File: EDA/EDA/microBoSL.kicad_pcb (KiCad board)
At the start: 4 copper layers, 40 x 13 mm, 54 parts, among them J1 Conn_01x04, J2 Conn_02x03_Odd_Even, J3 Conn_01x04, J4 Conn_01x04, J5 Conn_01x02, J6 Conn_01x10, J7 Conn_01x02, J8 USB_B_Micro, Q1 DMG2302UK, SW1 PTS636 SM43J SMTR LFS, U1 MAX40200ANS, U2 MAX40200ANS, U3 MCP1700-3302E_SOT23, U4 ATmega328-MMH, U5 MCP7940N-xSN, U6 74HC126PW-Q100, U7 FT232RQ, U8 Si4463, Y1 8MHz, Y2 32.768 kHz, Y3 30 MHz

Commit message: moved location on pcb of si4463
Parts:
- C10, C12: value C -> 5.1 pF
- C11: value C -> 6.8 pF
- C13: value C -> 12 pF
- C14: value C -> 18 pF
- C15: value C -> 9.1 pF
- L1: value L -> 220 nH
- L2: value L -> 68 nH
- L3: value L -> 24 nH
- L4: value L -> 27 nH
- L5, L6: value L -> 12 nH
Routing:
- net unconnected-(J6-Pad5): track 0.00 -> 13.1 mm, vias 0 -> 1
- net SS: track 13.1 -> 0.00 mm, vias 1 -> 0
- net unconnected-(J6-Pad1): track 0.00 -> 8.80 mm, vias 0 -> 1
- net I_RADIO: track 8.80 -> 0.00 mm, vias 1 -> 0
- net unconnected-(J6-Pad2): track 0.00 -> 6.88 mm, vias 0 -> 1
- net EN_RADIO: track 6.88 -> 0.00 mm, vias 1 -> 0
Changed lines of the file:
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@@
       (effects (font (size 1 1) (thickness 0.15)))
     )
-    (fp_text value "C" (at 0 1.16 90) (layer "F.Fab")
+    (fp_text value "5.1 pF" (at 0 1.16 90) (layer "F.Fab")
       (effects (font (size 1 1) (thickness 0.15)))
     )
@@
       (effects (font (size 1 1) (thickness 0.15)))
     )
-    (fp_text value "L" (at 0 1.17 90) (layer "F.Fab")
+    (fp_text value "24 nH" (at 0 1.17 90) (layer "F.Fab")
       (effects (font (size 1 1) (thickness 0.15)))
     )
@@
       (effects (font (size 1 1) (thickness 0.15)))
     )
-    (fp_text value "L" (at 0 1.17 90) (layer "F.Fab")
+    (fp_text value "12 nH" (at 0 1.17 90) (layer "F.Fab")
       (effects (font (size 1 1) (thickness 0.15)))
     )
@@
       (effects (font (size 1 1) (thickness 0.15)))
     )
-    (fp_text value "L" (at 0 1.17 90) (layer "F.Fab")
+    (fp_text value "27 nH" (at 0 1.17 90) (layer "F.Fab")
       (effects (font (size 1 1) (thickness 0.15)))
     )
@@
       (effects (font (size 1 1) (thickness 0.15)))
     )
-    (fp_text value "C" (at 0 1.16) (layer "F.Fab")
+    (fp_text value "18 pF" (at 0 1.16) (layer "F.Fab")
       (effects (font (size 1 1) (thickness 0.15)))
     )
@@
       (effects (font (size 1 1) (thickness 0.15)))
     )
-    (fp_text value "L" (at 0 1.17) (layer "F.Fab")
+    (fp_text value "68 nH" (at 0 1.17) (layer "F.Fab")
       (effects (font (size 1 1) (thickness 0.15)))
     )
@@
       (effects (font (size 1 1) (thickness 0.15)))
     )
-    (fp_text value "C" (at 0 1.16) (layer "F.Fab")
+    (fp_text value "9.1 pF" (at 0 1.16) (layer "F.Fab")
       (effects (font (size 1 1) (thickness 0.15)))
     )
@@
       (effects (font (size 1 1) (thickness 0.15)))
     )
-    (fp_text value "C" (at 0 1.16 90) (layer "F.Fab")
+    (fp_text value "6.8 pF" (at 0 1.16 90) (layer "F.Fab")
       (effects (font (size 1 1) (thickness 0.15)))
     )
@@
       (effects (font (size 1 1) (thickness 0.15)))
     )
-    (fp_text value "C" (at 0 1.16) (layer "F.Fab")
+    (fp_text value "5.1 pF" (at 0 1.16) (layer "F.Fab")
       (effects (font (size 1 1) (thickness 0.15)))
     )
@@
       (effects (font (size 1 1) (thickness 0.15)))
     )
-    (fp_text value "L" (at 0 1.17) (layer "F.Fab")
+    (fp_text value "220 nH" (at 0 1.17) (layer "F.Fab")
       (effects (font (size 1 1) (thickness 0.15)))
     )
@@
       (effects (font (size 1 1) (thickness 0.15)))
     )
-    (fp_text value "L" (at 0 1.17 90) (layer "F.Fab")
+    (fp_text value "12 nH" (at 0 1.17 90) (layer "F.Fab")
       (effects (font (size 1 1) (thickness 0.15)))
     )
@@
       (effects (font (size 1 1) (thickness 0.15)))
     )
-    (fp_text value "C" (at 0 1.16) (layer "F.Fab")
+    (fp_text value "12 pF" (at 0 1.16) (layer "F.Fab")
       (effects (font (size 1 1) (thickness 0.15)))
     )
@@
   (segment (start 107.7 110.7) (end 107.7 111.2) (width 0.8) (layer "B.Cu") (net 47))
   (segment (start 107.7 111.2) (end 107.319999 111.580001) (width 0.16) (layer "B.Cu") (net 47))
+  (segment (start 129.9 110.964661) (end 130.374774 111.439435) (width 0.16) (layer "F.Cu") (net 48))
+  (segment (start 129.9 110.4) (end 129.9 110.964661) (width 0.16) (layer "F.Cu") (net 48))
+  (segment (start 130.374774 111.439435) (end 130.374774 111.725226) (width 0.16) (layer "F.Cu") (net 48))
+  (via (at 130.374774 111.725226) (size 0.5) (drill 0.3) (layers "F.Cu" "B.Cu") (net 48))
+  (segment (start 130.374774 111.725226) (end 130.374774 111.590372) (width 0.16) (layer "In1.Cu") (net 48))
+  (segment (start 124.819999 107.154401) (end 124.819999 105.080001) (width 0.16) (layer "In1.Cu") (net 48))
+  (segment (start 126.829411 108.045009) (end 125.710607 108.045009) (width 0.16) (layer "In1.Cu") (net 48))
+  (segment (start 130.374774 111.590372) (end 126.829411 108.045009) (width 0.16) (layer "In1.Cu") (net 48))
+  (segment (start 125.750001 104.149999) (end 126.25 103.65) (width 0.16) (layer "In1.Cu") (net 48))
+  (segment (start 125.710607 108.045009) (end 124.819999 107.154401) (width 0.16) (layer "In1.Cu") (net 48))
+  (segment (start 124.819999 105.080001) (end 125.750001 104.149999) (width 0.16) (layer "In1.Cu") (net 48))
+  (segment (start 125.850226 106.653779) (end 125.850226 106.300226) (width 0.16) (layer "F.Cu") (net 49))
+  (segment (start 126.746447 107.55) (end 125.850226 106.653779) (width 0.16) (layer "F.Cu") (net 49))
+  (segment (start 127.5 107.55) (end 126.746447 107.55) (width 0.16) (layer "F.Cu") (net 49))
+  (via (at 125.850226 106.300226) (size 0.5) (drill 0.3) (layers "F.Cu" "B.Cu") (net 49))
+  (segment (start 124.25 104.7) (end 125.600227 106.050227) (width 0.16) (layer "B.Cu") (net 49))
+  (segment (start 125.600227 106.050227) (end 125.850226 106.300226) (width 0.16) (layer "B.Cu") (net 49))
+  (segment (start 122.44 103.65) (end 123.49 104.7) (width 0.16) (layer "B.Cu") (net 49))
+  (segment (start 123.49 104.7) (end 124.25 104.7) (width 0.16) (layer "B.Cu") (net 49))
+  (segment (start 127.5 106.649535) (end 127.112304 106.261839) (width 0.16) (layer "F.Cu") (net 50))
+  (segment (start 127.5 107.1) (end 127.5 106.649535) (width 0.16) (layer "F.Cu") (net 50))
+  (via (at 127.112304 106.261839) (size 0.5) (drill 0.3) (layers "F.Cu" "B.Cu") (net 50))
+  (segment (start 121.17 104.92) (end 122.020225 105.770225) (width 0.16) (layer "In2.Cu") (net 50))
+  (segment (start 121.17 103.65) (end 121.17 104.92) (width 0.16) (layer "In2.Cu") (net 50))
+  (segment (start 122.020225 105.770225) (end 126.670225 105.770225) (width 0.16) (layer "In2.Cu") (net 50))
+  (segment (start 127.112304 106.212304) (end 127.112304 106.261839) (width 0.16) (layer "In2.Cu") (net 50))
+  (segment (start 126.670225 105.770225) (end 127.112304 106.212304) (width 0.16) (layer "In2.Cu") (net 50))
   (segment (start 132.080543 110.480543) (end 132.080543 110.932748) (width 0.16) (layer "F.Cu") (net 53))
   (segment (start 131.4 109.8) (end 132.080543 110.480543) (width 0.16) (layer "F.Cu") (net 53))
@@
   (segment (start 127.05 107.6) (end 126.480001 107.030001) (width 0.16) (layer "In1.Cu") (net 55))
   (segment (start 131.266661 111.832711) (end 127.05 107.61605) (width 0.16) (layer "In1.Cu") (net 55))
-  (segment (start 129.9 110.964661) (end 130.374774 111.439435) (width 0.16) (layer "F.Cu") (net 56))
-  (segment (start 129.9 110.4) (end 129.9 110.964661) (width 0.16) (layer "F.Cu") (net 56))
-  (segment (start 130.374774 111.439435) (end 130.374774 111.725226) (width 0.16) (layer "F.Cu") (net 56))
-  (via (at 130.374774 111.725226) (size 0.5) (drill 0.3) (layers "F.Cu" "B.Cu") (net 56))
-  (segment (start 130.374774 111.725226) (end 130.374774 111.590372) (width 0.16) (layer "In1.Cu") (net 56))
-  (segment (start 124.819999 107.154401) (end 124.819999 105.080001) (width 0.16) (layer "In1.Cu") (net 56))
-  (segment (start 126.829411 108.045009) (end 125.710607 108.045009) (width 0.16) (layer "In1.Cu") (net 56))
-  (segment (start 130.374774 111.590372) (end 126.829411 108.045009) (width 0.16) (layer "In1.Cu") (net 56))
-  (segment (start 125.750001 104.149999) (end 126.25 103.65) (width 0.16) (layer "In1.Cu") (net 56))
-  (segment (start 125.710607 108.045009) (end 124.819999 107.154401) (width 0.16) (layer "In1.Cu") (net 56))
-  (segment (start 124.819999 105.080001) (end 125.750001 104.149999) (width 0.16) (layer "In1.Cu") (net 56))
-  (segment (start 125.850226 106.653779) (end 125.850226 106.300226) (width 0.16) (layer "F.Cu") (net 57))
-  (segment (start 126.746447 107.55) (end 125.850226 106.653779) (width 0.16) (layer "F.Cu") (net 57))
-  (segment (start 127.5 107.55) (end 126.746447 107.55) (width 0.16) (layer "F.Cu") (net 57))
-  (via (at 125.850226 106.300226) (size 0.5) (drill 0.3) (layers "F.Cu" "B.Cu") (net 57))
-  (segment (start 124.25 104.7) (end 125.600227 106.050227) (width 0.16) (layer "B.Cu") (net 57))
-  (segment (start 125.600227 106.050227) (end 125.850226 106.300226) (width 0.16) (layer "B.Cu") (net 57))
-  (segment (start 122.44 103.65) (end 123.49 104.7) (width 0.16) (layer "B.Cu") (net 57))
-  (segment (start 123.49 104.7) (end 124.25 104.7) (width 0.16) (layer "B.Cu") (net 57))
-  (segment (start 127.5 106.649535) (end 127.112304 106.261839) (width 0.16) (layer "F.Cu") (net 58))
-  (segment (start 127.5 107.1) (end 127.5 106.649535) (width 0.16) (layer "F.Cu") (net 58))
-  (via (at 127.112304 106.261839) (size 0.5) (drill 0.3) (layers "F.Cu" "B.Cu") (net 58))
-  (segment (start 121.17 104.92) (end 122.020225 105.770225) (width 0.16) (layer "In2.Cu") (net 58))
-  (segment (start 121.17 103.65) (end 121.17 104.92) (width 0.16) (layer "In2.Cu") (net 58))
-  (segment (start 122.020225 105.770225) (end 126.670225 105.770225) (width 0.16) (layer "In2.Cu") (net 58))
-  (segment (start 127.112304 106.212304) (end 127.112304 106.261839) (width 0.16) (layer "In2.Cu") (net 58))
-  (segment (start 126.670225 105.770225) (end 127.112304 106.212304) (width 0.16) (layer "In2.Cu") (net 58))
   (segment (start 112.885 70.075) (end 113.92 71.11) (width 0.2) (layer "F.Cu") (net 78))
   (segment (start 112.475 70.075) (end 112.885 70.075) (width 0.2) (layer "F.Cu") (net 78))

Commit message: laying out pcb
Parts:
- removed U5: MCP7940N-xSN, Package_DFN_QFN:DFN-8-1EP_3x2mm_P0.5mm_EP1.3x1.5mm
- added C16: 100 nF, Capacitor_SMD:C_0402_1005Metric, B.Cu at (132.5, 104.4)
- added C17: 15 pF, Capacitor_SMD:C_0402_1005Metric, B.Cu at (136.3, 110.7)
- added C18: 15 pF, Capacitor_SMD:C_0402_1005Metric, B.Cu at (136.3, 106.9)
- added D4: CUS08F30,H3F, Diode_SMD:D_SOD-323, B.Cu at (114.6, 129.1)
- added F1: 1A, Fuse:Fuse_1206_3216Metric_Pad1.42x1.75mm_HandSolder, B.Cu at (109.2, 124.3)
- added J9: MOTOR_OUT, Connector_PinHeader_2.54mm:PinHeader_1x02_P2.54mm_Vertical, F.Cu at (165.6, 132.8)
- added Q2: DMP2165UW, Package_TO_SOT_SMD:SOT-323_SC-70, B.Cu at (113.6, 121.9)
- added R10: 10 kΩ, Resistor_SMD:R_0402_1005Metric, B.Cu at (130.0, 108.9)
- added R11: 4.7 MΩ, Capacitor_SMD:C_0402_1005Metric, B.Cu at (132.3, 102.1)
- added R12: 4.7 MΩ, Capacitor_SMD:C_0402_1005Metric, B.Cu at (132.3, 100.2)
- added R9: 10 kΩ, Resistor_SMD:R_0402_1005Metric, B.Cu at (128.8, 109.4)
- added SW2: EG1215AA, SIMFootprints:EG1215AA, F.Cu at (117.2, 122.2)
- C1: value 1 μF -> 2.2 μF; footprint Capacitor_SMD:C_1206_3216Metric -> Capacitor_SMD:C_0805_2012Metric
- C4: value 12 pF -> 100 nF
- C5: value 12 pF -> 100 nF; moved to B.Cu
- C6, R3, R5: moved to B.Cu
- J2: value Conn_02x03_Odd_Even -> Conn_01x03; footprint Connector_PinHeader_2.54mm:PinHeader_2x03_P2.54mm_Vertical -> Connector_PinHeader_2.54mm:PinHeader_1x03_P2.54mm_Vertical
- J6: value Conn_01x10 -> Conn_01x03; footprint Connector_PinHeader_1.27mm:PinHeader_1x10_P1.27mm_Vertical -> Connector_PinHeader_2.54mm:PinHeader_1x03_P2.54mm_Vertical
- J7: value Conn_01x02 -> Conn_01x03; footprint Connector_PinHeader_2.54mm:PinHeader_1x02_P2.54mm_Vertical -> Connector_PinHeader_2.54mm:PinHeader_1x03_P2.54mm_Vertical
- Q1: value DMG2302UK -> DMP2165UW; footprint Package_TO_SOT_SMD:SOT-23 -> Package_TO_SOT_SMD:SOT-323_SC-70
- R2: value 1 kΩ -> 10 kΩ
- R4: value 10 kΩ -> 4.7 MΩ; footprint Resistor_SMD:R_0402_1005Metric -> Capacitor_SMD:C_0402_1005Metric; moved to B.Cu
- SW1: value PTS636 SM43J SMTR LFS -> RST; footprint SIMFootprints:PTS636 SM43J SMTR LFS -> Jumper:SolderJumper-2_P1.3mm_Open_RoundedPad1.0x1.5mm; moved to B.Cu
- U1: value MAX40200ANS -> TPS709A33DBVT; footprint Package_BGA:WLP-4_0.73x0.73mm_Layout2x2_P0.35mm_Ball0.22mm_Pad0.2mm_NSMD -> Package_TO_SOT_SMD:SOT-23-5
- U2: value MAX40200ANS -> ZXBM5210-S; footprint Package_BGA:WLP-4_0.73x0.73mm_Layout2x2_P0.35mm_Ball0.22mm_Pad0.2mm_NSMD -> Package_SO:SOIC-8_3.9x4.9mm_P1.27mm
- U3: value MCP1700-3302E_SOT23 -> MCP7940N-xMNY; footprint Package_TO_SOT_SMD:SOT-23 -> Package_DFN_QFN:DFN-8-1EP_3x2mm_P0.5mm_EP1.36x1.46mm
- Y2: footprint Crystal:Crystal_SMD_EuroQuartz_EQ161-2Pin_3.2x1.5mm -> Crystal:Crystal_SMD_2012-2Pin_2.0x1.2mm; moved to B.Cu
- moved AE1 95.1 mm to (174.3, 123.6), turned to 90 degrees
- moved C15 91.8 mm to (172.0, 123.1), turned to 90 degrees
- moved L6 89.8 mm to (170.6, 123.5), turned to 0 degrees
- moved C14 87.7 mm to (169.1, 123.1), turned to 90 degrees
- moved L5 85.7 mm to (167.6, 123.5), turned to 0 degrees
- moved C13 83.6 mm to (166.2, 123.1), turned to 90 degrees
- moved L3 83.0 mm to (165.7, 124.5), turned to 0 degrees
- moved L4 81.9 mm to (164.8, 126.5), turned to 0 degrees
- moved C12 81.8 mm to (164.8, 125.5), turned to 180 degrees
- moved C10 81.4 mm to (164.3, 127.9), turned to -90 degrees
- moved C11 80.3 mm to (163.8, 124.5), turned to 180 degrees
- moved L2 79.8 mm to (163.4, 126.0), turned to 90 degrees
- moved L1 79.6 mm to (163.4, 123.1), turned to -90 degrees
- moved C9 77.1 mm to (161.6, 122.3), turned to 0 degrees
- moved C8 77.1 mm to (161.6, 121.2), turned to 0 degrees
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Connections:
- C4 pad 2: Net-(C4-Pad2) -> V_3.3
- C5 pad 1: GND -> VBAT
- C5 pad 2: Net-(C5-Pad2) -> GND
- J2 pad 1: GND -> D7
- J2 pad 2: GND -> A1
- J2 pad 3: Hall_WKE_P -> A3
- J5 pad 2: VPP -> Net-(J5-Pad2)
- J6 pad 1: unconnected-(J6-Pad1) -> Hall_CNT_S
- J6 pad 2: unconnected-(J6-Pad2) -> GND
- J6 pad 3: D7 -> Hall_CNT_P
- J7 pad 1: Net-(J7-Pad1) -> Hall_WKE_S
- Q1 pad 1: MOSFET -> Net-(Q1-Pad1)
- Q1 pad 2: GND -> Net-(D4-Pad1)
- Q1 pad 3: Net-(J7-Pad1) -> VBAT
- R2 pad 1: GND -> Net-(Q1-Pad1)
- R2 pad 2: MOSFET -> USB_V
- R3 pad 1: SCL -> Net-(R3-Pad1)
- R3 pad 2: V_3.3 -> VPP
- R4 pad 1: V_3.3 -> GND
- R4 pad 2: SDA -> Net-(Q1-Pad1)
- U3 pad 1: GND -> Net-(C18-Pad2)
- U3 pad 2: V_3.3 -> Net-(C17-Pad2)
- U3 pad 3: Net-(U1-PadA2) -> Net-(C16-Pad1)
- U4 pad 10: D8 -> MREV
- U4 pad 11: MOSFET -> MFWD
- Y2 pad 1: Net-(C4-Pad2) -> Net-(C18-Pad2)
- Y2 pad 2: Net-(C5-Pad2) -> Net-(C17-Pad2)
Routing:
- net GND: track 85.8 -> 4.77 mm, vias 12 -> 5
- net V_3.3: track 75.2 -> 10.1 mm, vias 3 -> 0
- net VPP: track 43.6 -> 0.00 mm
- net SCL: track 35.5 -> 0.00 mm, vias 3 -> 0
- net TTL_3.3V: track 33.1 -> 0.00 mm, vias 3 -> 0
- net TLL_RST: track 30.6 -> 0.00 mm, vias 1 -> 0
- net TLL_RX: track 23.8 -> 0.00 mm, vias 2 -> 0
- net TLL_TX: track 22.4 -> 0.00 mm, vias 1 -> 0
- net SDA: track 22.2 -> 0.00 mm, vias 2 -> 0
- net AND_TX: track 21.6 -> 0.00 mm, vias 2 -> 0
- net USB_V: track 20.0 -> 0.00 mm, vias 2 -> 0
- net Hall_CNT_P: track 19.7 -> 0.00 mm, vias 1 -> 0
- net Hall_WKE_P: track 18.8 -> 0.00 mm, vias 1 -> 0
- net MOSI: track 15.0 -> 0.00 mm, vias 1 -> 0
- net MOSFET: track 13.7 -> 0.00 mm, vias 1 -> 0
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- removed copper zone on In1.Cu, net GND
- removed copper zone on In2.Cu, net GND
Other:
- board size 40 x 13 mm -> 69.5 x 15 mm
- board text added: "FUSE:1A"
- board text added: "microBoSL rev 0.3.0R"
- board text removed: "microBoSL rev 0.1.0"

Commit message: more work on PCB layout
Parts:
- C2, C3, Y1: moved to F.Cu
- moved U2 51.2 mm to (140.7, 131.7)
- moved J4 21.3 mm to (118.7, 141.0)
- moved AE1 16.0 mm to (158.3, 123.6)
- moved C10 16.0 mm to (148.3, 127.9)
- moved C11 16.0 mm to (147.8, 124.5)
- moved C12 16.0 mm to (148.8, 125.5)
- moved C13 16.0 mm to (150.2, 123.1)
- moved C14 16.0 mm to (153.1, 123.1)
- moved C15 16.0 mm to (156.0, 123.1)
- moved C8 16.0 mm to (145.6, 121.2)
- moved C9 16.0 mm to (145.6, 122.3)
- moved J2 16.0 mm to (158.3, 129.2)
- moved J7 16.0 mm to (158.3, 132.8)
- moved J9 16.0 mm to (149.6, 132.8)
- moved L1 16.0 mm to (147.4, 123.1)
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
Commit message: finished component placement
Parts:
- C17, C18, C5, R10, R9, U3, Y2: moved to F.Cu
- C4: moved to B.Cu
- moved C4 40.3 mm to (136.7, 128.1), turned to 0 degrees
- moved R12 29.2 mm to (133.3, 129.3)
- moved R11 28.3 mm to (134.3, 130.4)
- moved C16 23.7 mm to (133.3, 128.1)
- moved R1 21.5 mm to (121.5, 124.6), turned to 180 degrees
- moved J9 21.1 mm to (132.0, 121.3)
- moved J4 20.3 mm to (137.2, 132.8)
- moved J6 16.9 mm to (141.6, 132.8)
- moved C18 16.1 mm to (125.0, 129.8), turned to 90 degrees
- moved C2 15.9 mm to (137.9, 126.3), turned to 180 degrees
- moved Y2 13.6 mm to (126.9, 129.8), turned to 0 degrees
- moved Y1 13.3 mm to (138.0, 128.9), turned to -90 degrees
- moved C3 12.0 mm to (135.6, 130.0), turned to 90 degrees
- moved C17 11.1 mm to (128.8, 129.8), turned to 90 degrees
- moved U2 9.23 mm to (136.7, 123.4), turned to -90 degrees
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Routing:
- net V_3.3: track 10.1 -> 9.14 mm
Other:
- board size 69.5 x 15 mm -> 52 x 15 mm

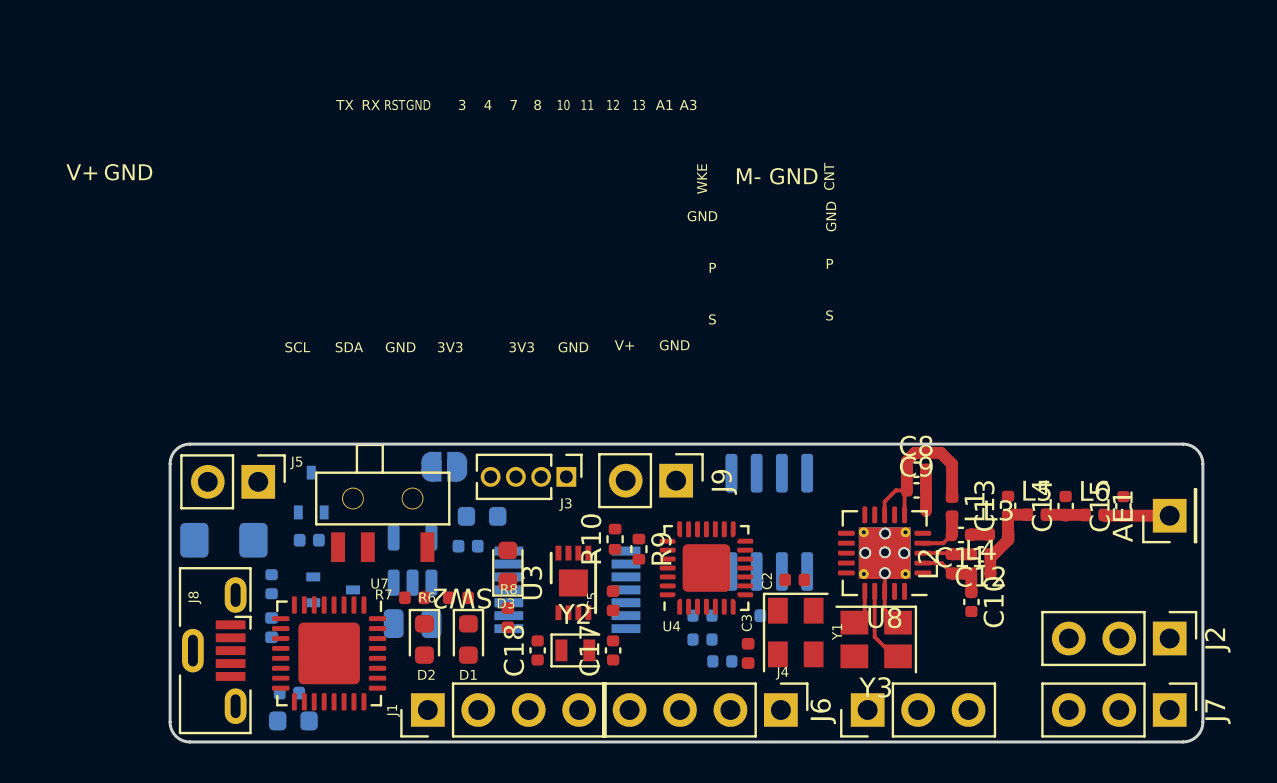
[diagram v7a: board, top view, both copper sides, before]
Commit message: added BOM and finished most layout
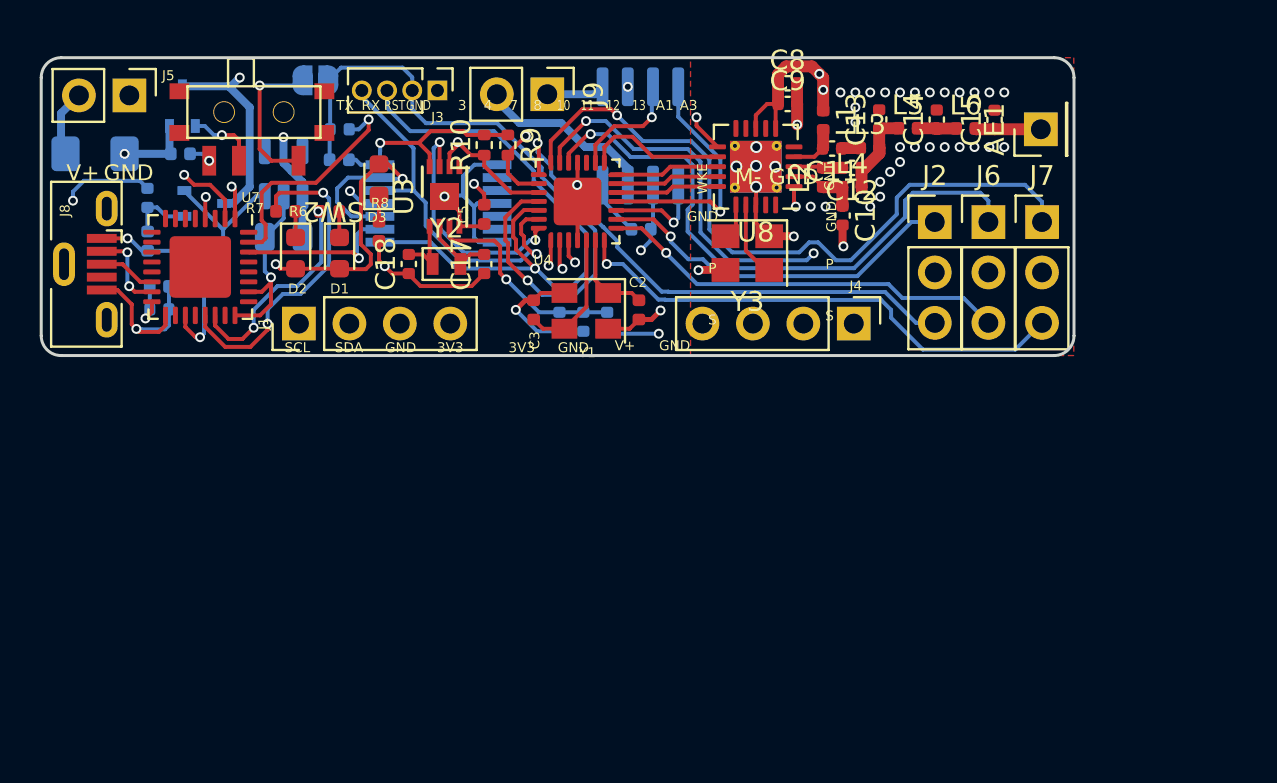
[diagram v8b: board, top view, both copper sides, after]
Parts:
- C6, C7: footprint Capacitor_SMD:C_0603_1608Metric -> Capacitor_SMD:C_0402_1005Metric
- moved J7 25.4 mm to (150.4, 108.3), turned to 0 degrees
- moved J6 25.3 mm to (147.7, 108.3), turned to 0 degrees
- moved J2 24.1 mm to (145.0, 108.3), turned to 0 degrees
- moved C6 21.8 mm to (106.0, 112.7)
- moved R5 21.5 mm to (106.0, 111.5)
- moved R9 21.4 mm to (123.5, 104.4)
- moved R10 20.9 mm to (122.3, 104.4)
- moved C7 20.8 mm to (115.0, 103.6)
- moved C14 20.5 mm to (145.1, 103.1)
- moved C9 20.5 mm to (137.6, 102.3)
- moved J8 20.5 mm to (102.2, 110.4)
- moved L3 20.5 mm to (141.7, 104.5)
- moved L6 20.5 mm to (146.6, 103.6)
- moved SW2 20.5 mm to (110.7, 102.7)
- moved Y3 20.5 mm to (135.6, 109.8)
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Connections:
- J8 pad 6: unconnected-(J8-Pad6) -> (no net)
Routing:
- net GND: track 4.86 -> 82.5 mm, vias 5 -> 48
- net VPP: track 0.00 -> 50.5 mm, vias 0 -> 2
- net TTL_3.3V: track 0.00 -> 44.3 mm, vias 0 -> 4
- net VBAT: track 0.00 -> 37.9 mm, vias 0 -> 3
- net Hall_WKE_S: track 0.00 -> 35.6 mm, vias 0 -> 1
- net TLL_RST: track 0.00 -> 35.1 mm, vias 0 -> 1
- net TLL_RX: track 0.00 -> 31.8 mm, vias 0 -> 1
- net Hall_CNT_S: track 0.00 -> 30.4 mm, vias 0 -> 1
- net V_3.3: track 9.14 -> 36.6 mm, vias 0 -> 7
- net A3: track 0.00 -> 26.1 mm, vias 0 -> 1
- net A1: track 0.00 -> 25.7 mm, vias 0 -> 2
- net Hall_WKE_P: track 0.00 -> 25.7 mm, vias 0 -> 1
- net SCL: track 0.00 -> 21.4 mm, vias 0 -> 1
- net Hall_CNT_P: track 0.00 -> 20.7 mm, vias 0 -> 1
- net TLL_TX: track 0.00 -> 19.3 mm, vias 0 -> 1
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- added copper zone on F.Cu, net GND
- added copper zone on In1.Cu, net GND
- added copper zone on In2.Cu, net V_3.3
